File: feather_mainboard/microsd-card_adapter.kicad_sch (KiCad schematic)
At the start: 10 parts, among them J2 MEM2090-00-145-00-A

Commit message: schematic is almost done (check TODOs in schematic file)
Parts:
- removed J2: MEM2090-00-145-00-A, Custom footprints:MEM20900014500A, symbol MEM2090-00-145-00-A:MEM2090-00-145-00-A
- removed R19, R20, R21: 10kΩ, Resistor_SMD:R_0805_2012Metric_Pad1.20x1.40mm_HandSolder, symbol Device:R
- added J3: 693071020811, Custom footprints:693071020811, symbol 693071020811:693071020811
- added R15, R16, R17: 10kΩ, Resistor_SMD:R_0805_2012Metric_Pad1.20x1.40mm_HandSolder, symbol Device:R
- renumbered C8 to C11, C9 to C12, R16 to R12, R17 to R13, R18 to R14
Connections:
- net GND: now also J3.10 (GND), J3.11 (GND__1), J3.12 (GND__2), J3.13 (GND__3)
- net SD_CD: now also J3.9 (CDSW1), R17.1
- net SD_CLK: now also J3.5 (CLK)
- net SD_CS/DAT3: now also J3.2 (CD/DAT3)
- net SD_DAT1: now also J3.8 (DAT1), R15.2
- net SD_DAT2: now also J3.1 (DAT2)
- net SD_GND: now also J3.6 (VSS)
- net SD_MISO/CMD: now also J3.3 (CMD)
- net SD_MOSI/DAT0: now also J3.7 (DAT0), R16.2
- net SD_VCC: now also J3.4 (VDD)
- net VCC: now also R15.1, R16.1, R17.2
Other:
- moved on the sheet: C11, C12

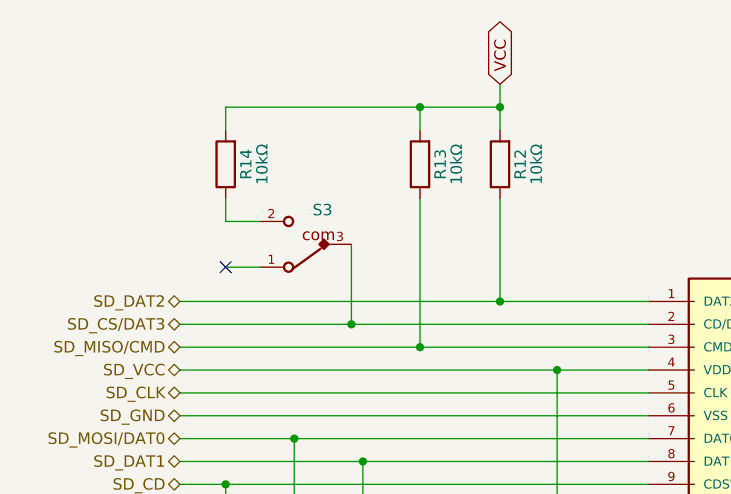
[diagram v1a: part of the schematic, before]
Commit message: changed footprints location to match the new folder. TODO: check if the path is working on another computer
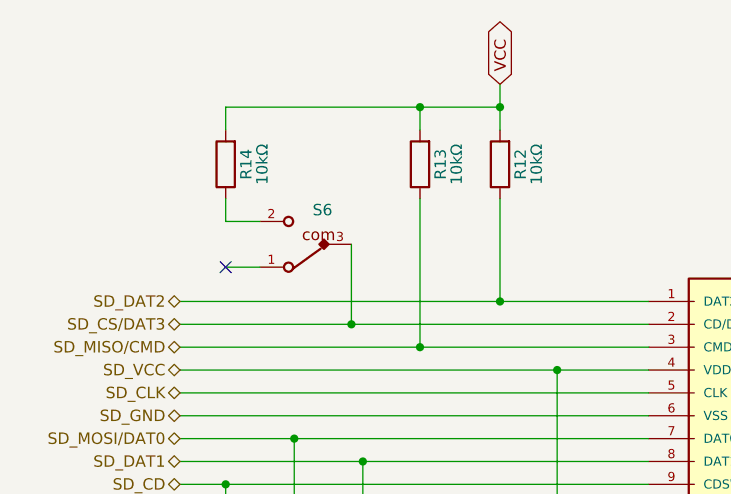
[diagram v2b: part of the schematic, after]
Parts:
- C11, C12: footprint footprints:WCAP-CSGP_1210_H2.0 -> Custom footprints:WCAP-CSGP_1210_H2.0
- renumbered S3 to S6
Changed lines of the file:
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@@
 			)
 		)
-		(property "Footprint" "footprints:WCAP-CSGP_1210_H2.0"
+		(property "Footprint" "Custom footprints:WCAP-CSGP_1210_H2.0"
 			(at 121.92 123.19 0)
 			(effects
@@
 	)
 	(symbol
+		(lib_name "WCAP-CSGP_1210_H2.0_1")
 		(lib_id "WCAP-CSGP_1210_H2.0:WCAP-CSGP_1210_H2.0")
 		(at 130.81 123.19 270)
@@
 			)
 		)
-		(property "Footprint" "footprints:WCAP-CSGP_1210_H2.0"
+		(property "Footprint" "Custom footprints:WCAP-CSGP_1210_H2.0"
 			(at 130.81 123.19 0)
 			(effects
@@
 		(on_board yes)
 		(dnp no)
-		(property "Reference" "S3"
+		(property "Reference" "S6"
 			(at 103.632 81.28 0)
 			(effects
@@
 			(project "feather_mainboard"
 				(path "/e1e12730-ab4f-45db-8b66-c1e0f78e2f00/6bb461df-e058-49ab-990d-543fb2df67dd"
-					(reference "S3")
+					(reference "S6")
 					(unit 1)
 				)

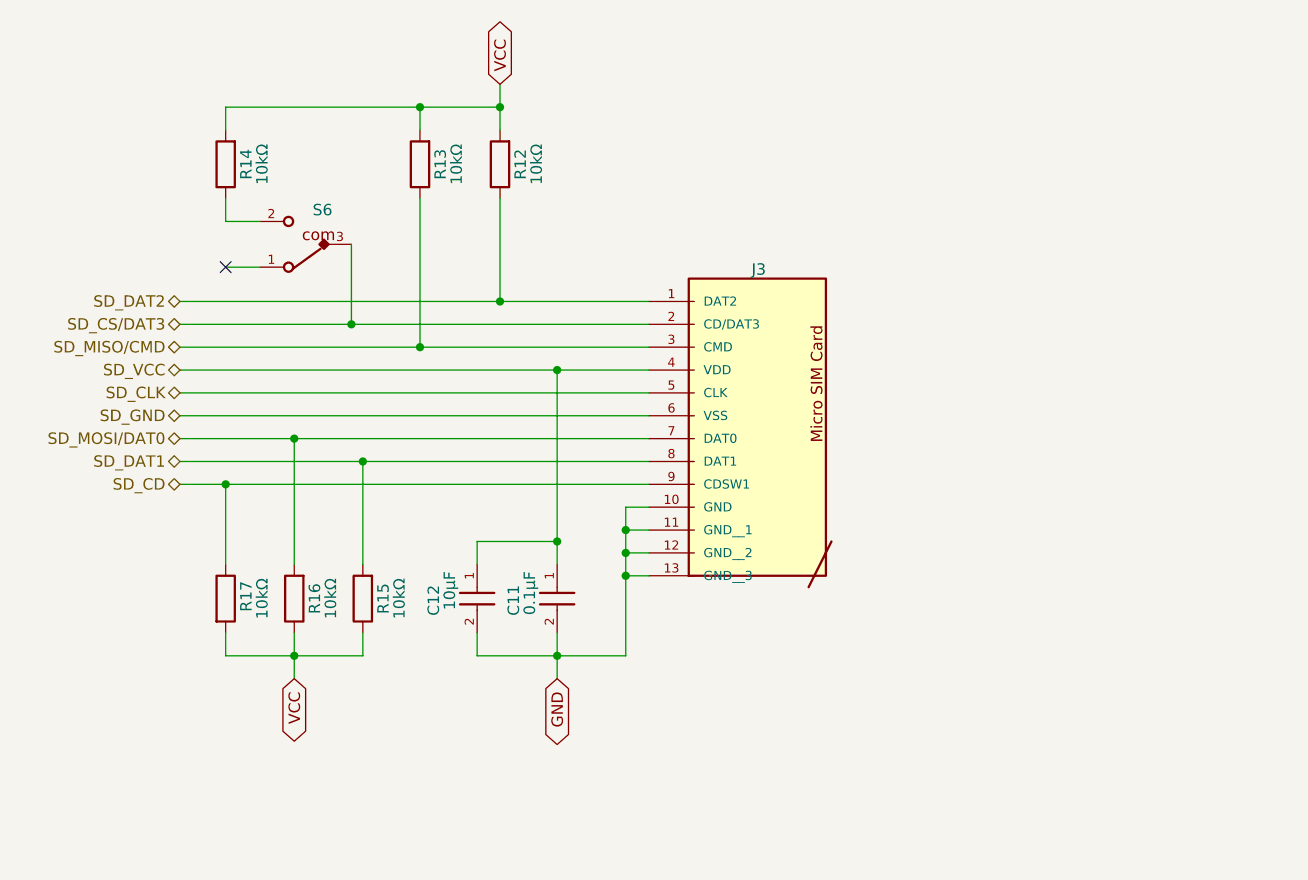
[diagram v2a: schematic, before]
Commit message: added daughter board
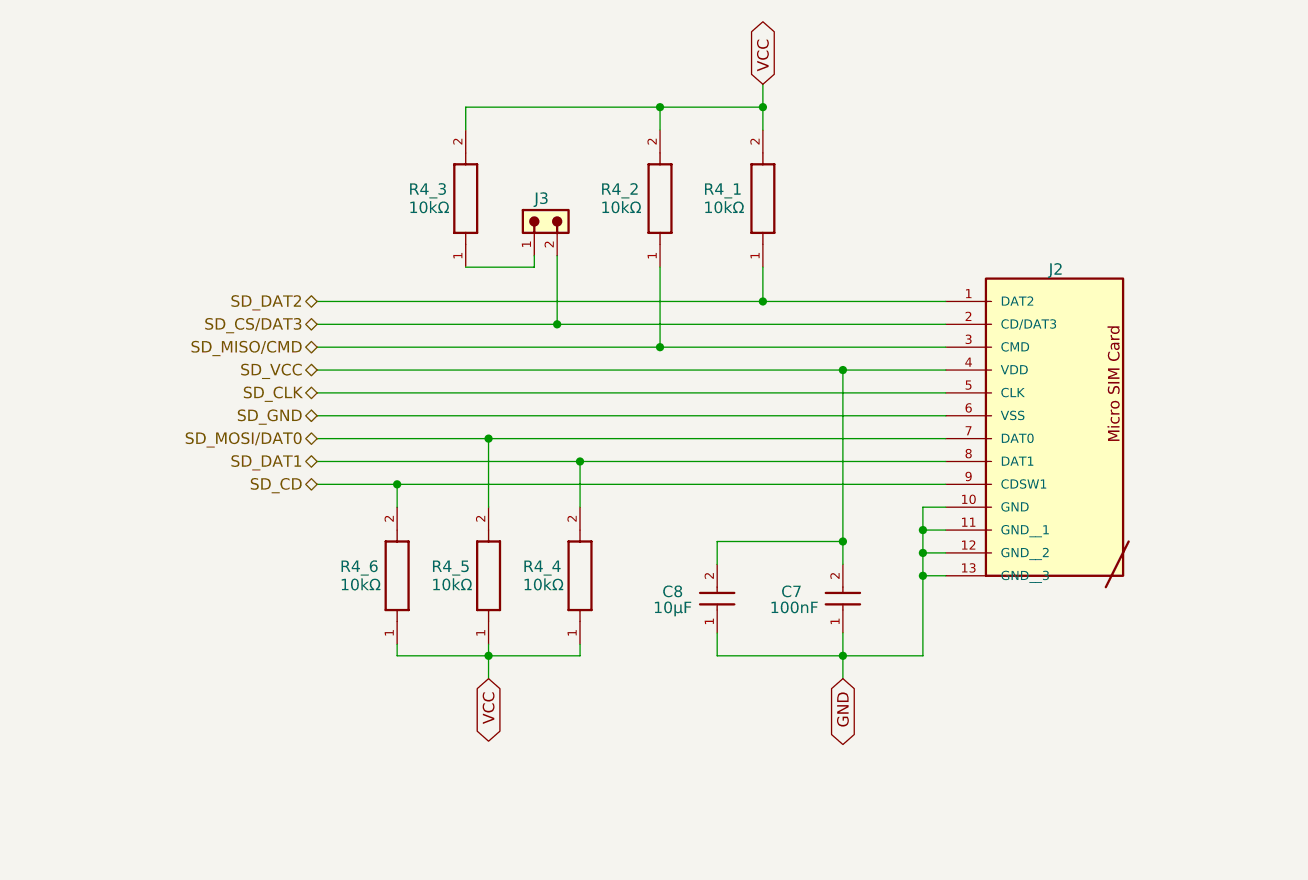
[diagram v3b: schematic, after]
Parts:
- removed C11: 0.1µF, Custom footprints:WCAP-CSGP_1210_H2.0, symbol WCAP-CSGP_1210_H2.0:WCAP-CSGP_1210_H2.0
- removed C12: 10µF, Custom footprints:WCAP-CSGP_1210_H2.0, symbol WCAP-CSGP_1210_H2.0:WCAP-CSGP_1210_H2.0
- removed R12, R13, R14, R15, R16, R17: 10kΩ, Resistor_SMD:R_0805_2012Metric_Pad1.20x1.40mm_HandSolder, symbol Device:R
- removed S6: 450405020524, Custom footprints:450405020524, symbol 450405020524:450405020524
- added C7: 100nF, Custom footprints:WCAP-CSGP_0603_R, symbol WCAP-CSGP_0603:WCAP-CSGP_0603
- added C8: 10µF, Custom footprints:WCAP-CSGP_0603_R, symbol WCAP-CSGP_0603:WCAP-CSGP_0603
- added J3: 61300211121, Custom footprints:61300211121, symbol 6130XX11121_61300211121:6130XX11121_61300211121
- added R4_1, R4_2, R4_3, R4_4, R4_5, R4_6: 10kΩ, Custom footprints:WRIS-RSKS_0603_REFLOW, symbol WRIS-RSKS_0603:WRIS-RSKS_0603
- renumbered J3 to J2
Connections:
- net GND: now also C7.1, C8.1
- net SD_CD: now also R4_6.2
- net SD_CS/DAT3: now also J3.2
- net SD_DAT1: now also R4_4.2
- net SD_DAT2: now also R4_1.1
- net SD_MISO/CMD: now also R4_2.1
- net SD_MOSI/DAT0: now also R4_5.2
- net SD_VCC: now also C7.2, C8.2
- net VCC: now also R4_1.2, R4_2.2, R4_3.2, R4_4.1, R4_5.1, R4_6.1
- new net: J3.1, R4_3.1
- no-connect marks 1 -> 0
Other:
- moved on the sheet: J2

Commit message: finished mainboard design, need to do the routing
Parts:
- renumbered C7 to C1_4, C8 to C2_2, J2 to J4, J3 to J5, R4_5 to R1_10, R4_6 to R1_11, R4_1 to R1_6, R4_2 to R1_7, R4_3 to R1_8, R4_4 to R1_9
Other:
- moved on the sheet: C1_4, C2_2, J4, R1_10, R1_11, R1_6, R1_7, R1_8, R1_9

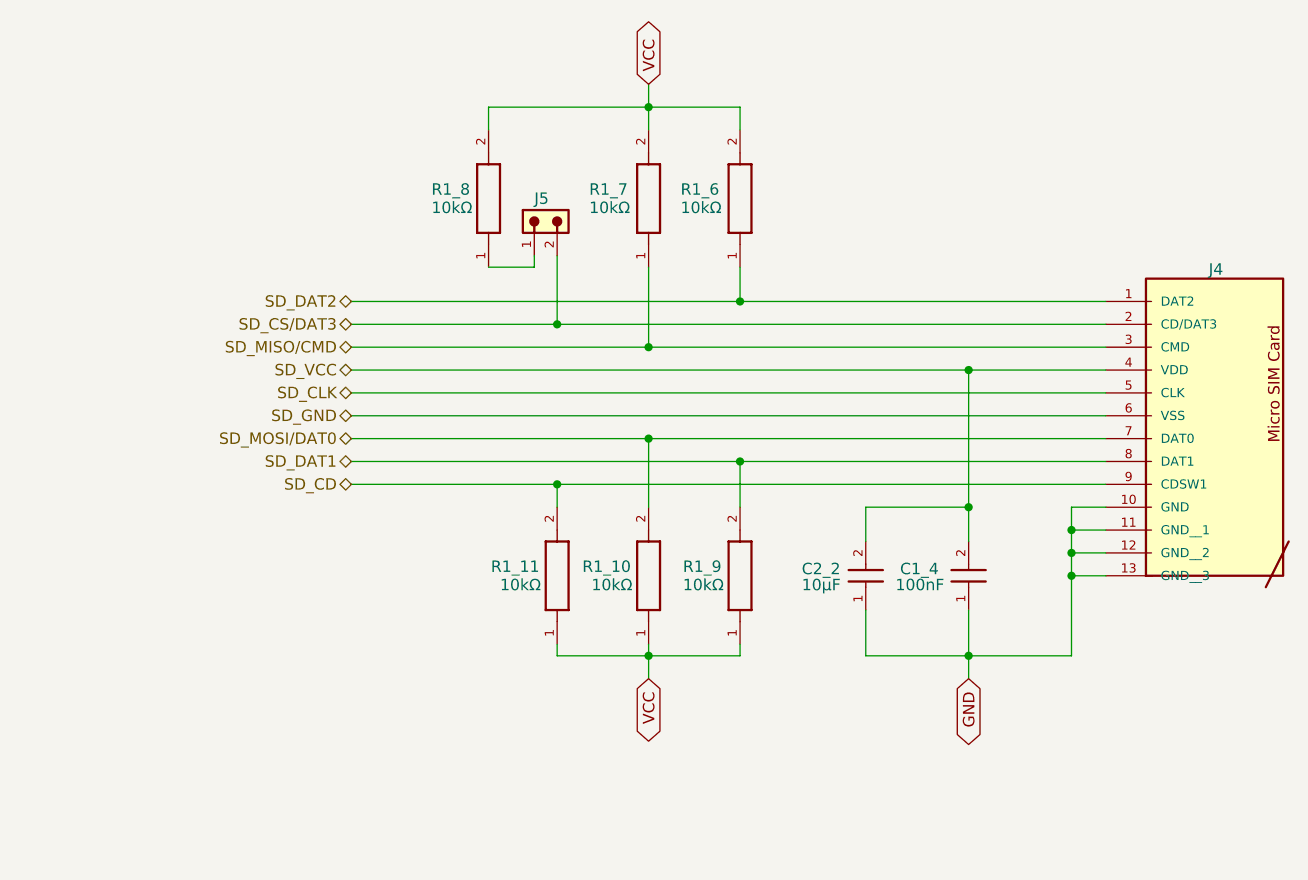
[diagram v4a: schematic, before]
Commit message: added pins for the sd connections
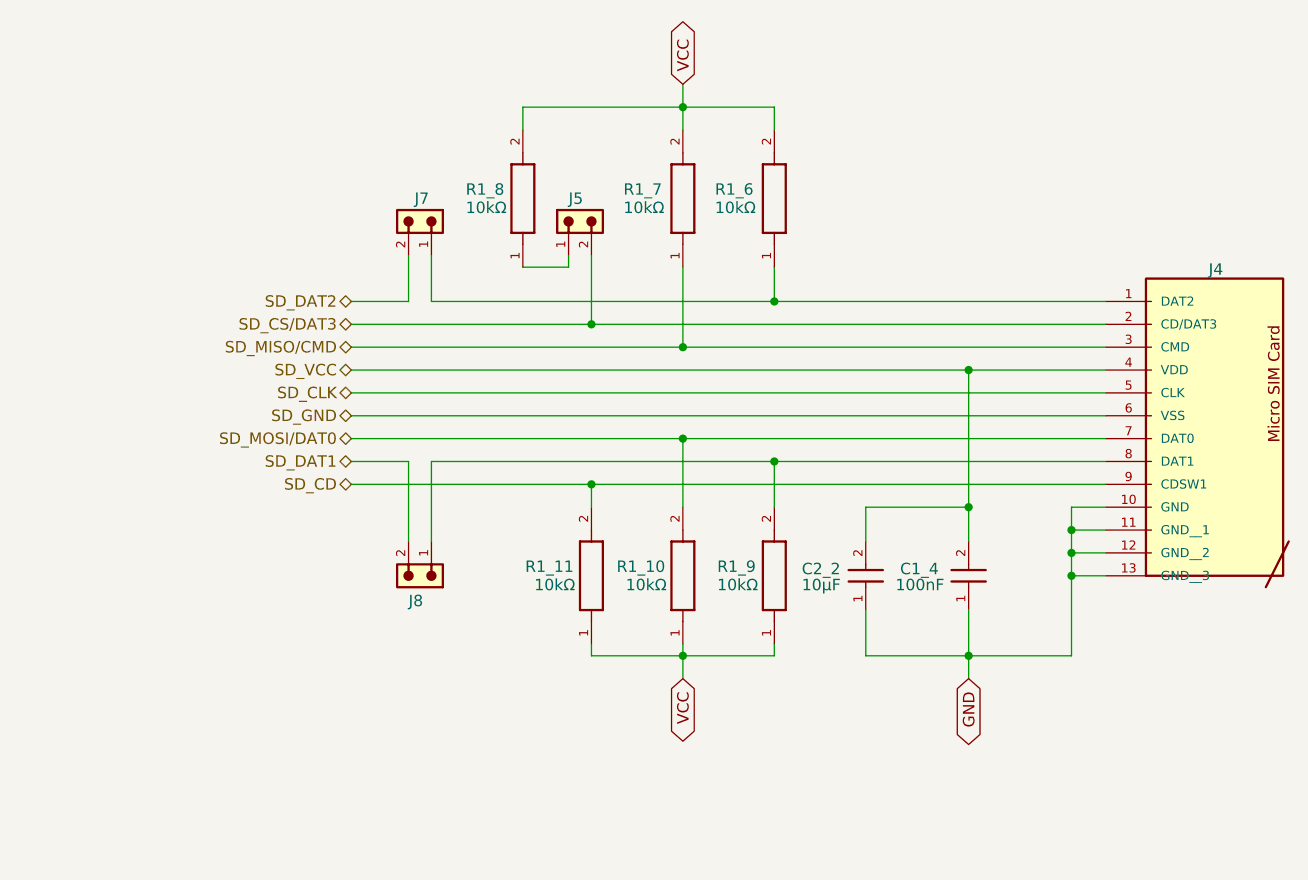
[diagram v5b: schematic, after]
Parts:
- added J7, J8: 61300211121, Custom footprints:61300211121, symbol 6130XX11121_61300211121:6130XX11121_61300211121
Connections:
- net SD_DAT1: now also J8.2; no longer J4.8 (DAT1), R1_9.2
- net SD_DAT2: now also J7.2; no longer J4.1 (DAT2), R1_6.1
- new net: J4.8 (DAT1), J8.1, R1_9.2
- new net: J4.1 (DAT2), J7.1, R1_6.1
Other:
- moved on the sheet: J5, R1_10, R1_11, R1_6, R1_7, R1_8, R1_9

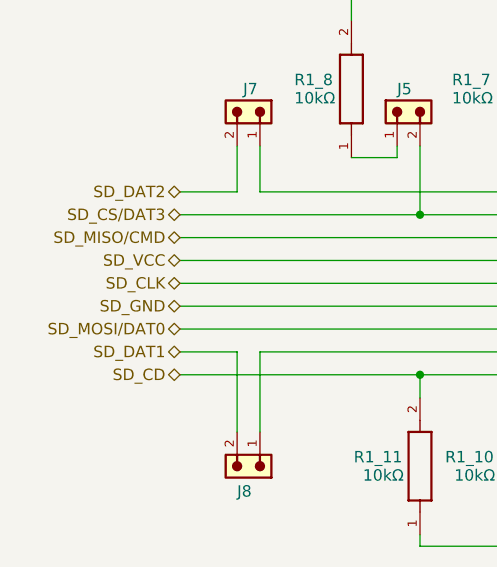
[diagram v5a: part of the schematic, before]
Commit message: Corrected/switched the names of MISO and MOSI pins
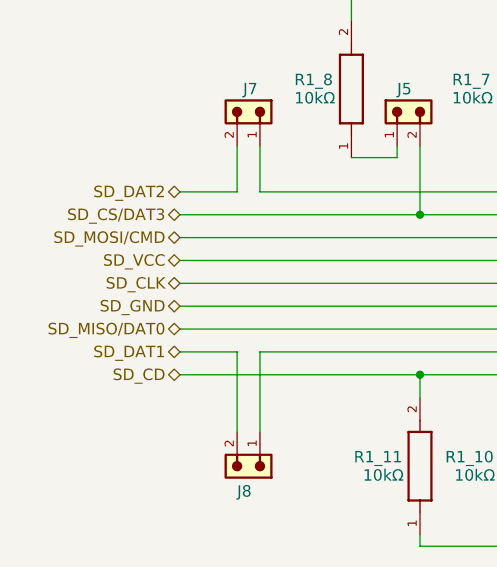
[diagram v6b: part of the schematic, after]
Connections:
- net SD_MISO/CMD renamed SD_MOSI/CMD
- net SD_MOSI/DAT0 renamed SD_MISO/DAT0
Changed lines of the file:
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@@
 		)
 	)
-	(hierarchical_label "SD_MOSI{slash}DAT0"
+	(hierarchical_label "SD_MISO{slash}DAT0"
 		(shape bidirectional)
 		(at 107.95 106.68 180)
@@
 		)
 	)
-	(hierarchical_label "SD_MISO{slash}CMD"
+	(hierarchical_label "SD_MOSI{slash}CMD"
 		(shape bidirectional)
 		(at 107.95 96.52 180)

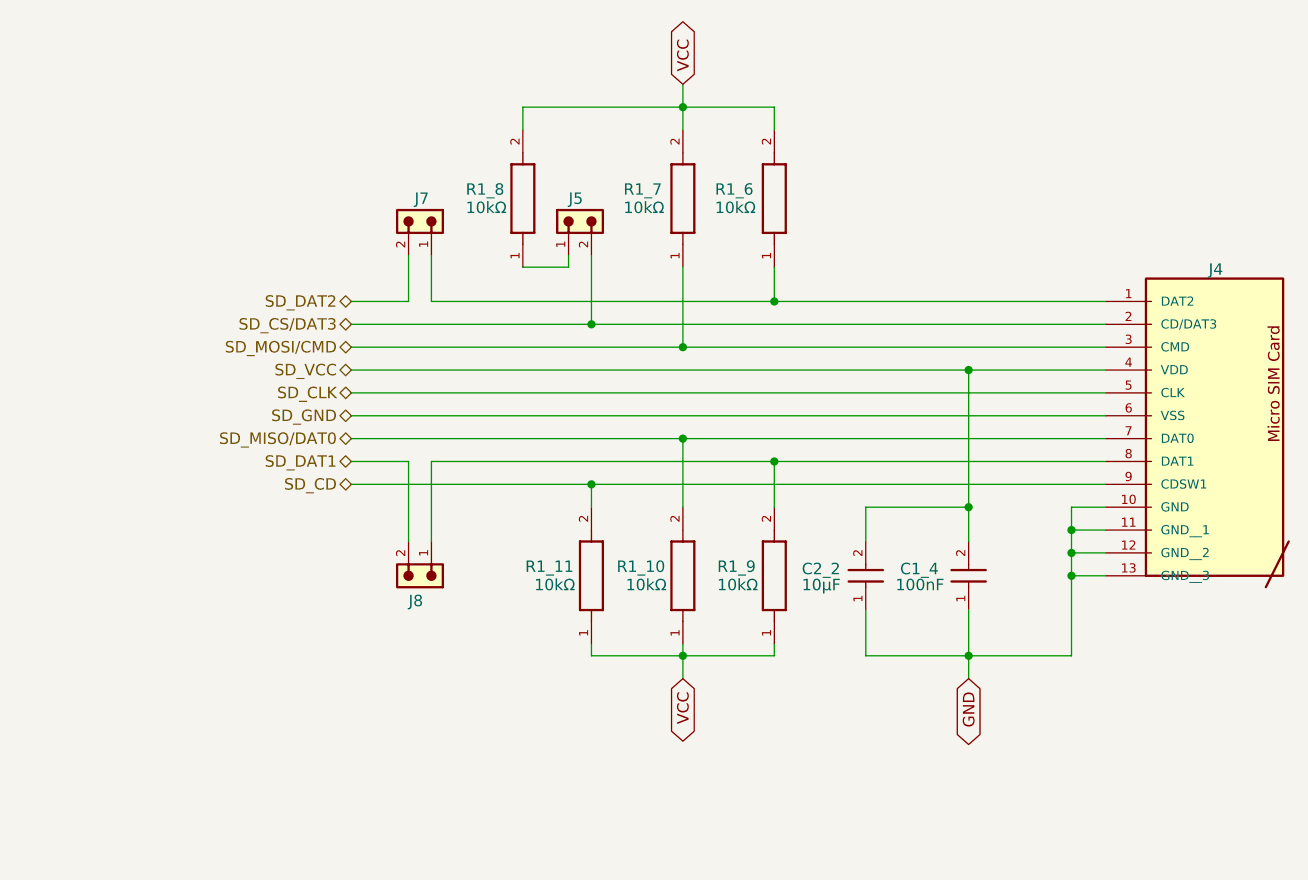
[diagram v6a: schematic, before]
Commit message: Added V1.1: added a Shottky diode to block the parasitic feedback into the system from the SD adapter; routed the SD adapter pull-ups to the SD Vcc and not the uC Vcc; updated silkscreen text; cleaned routing overall; more vias and more ground plane coverage
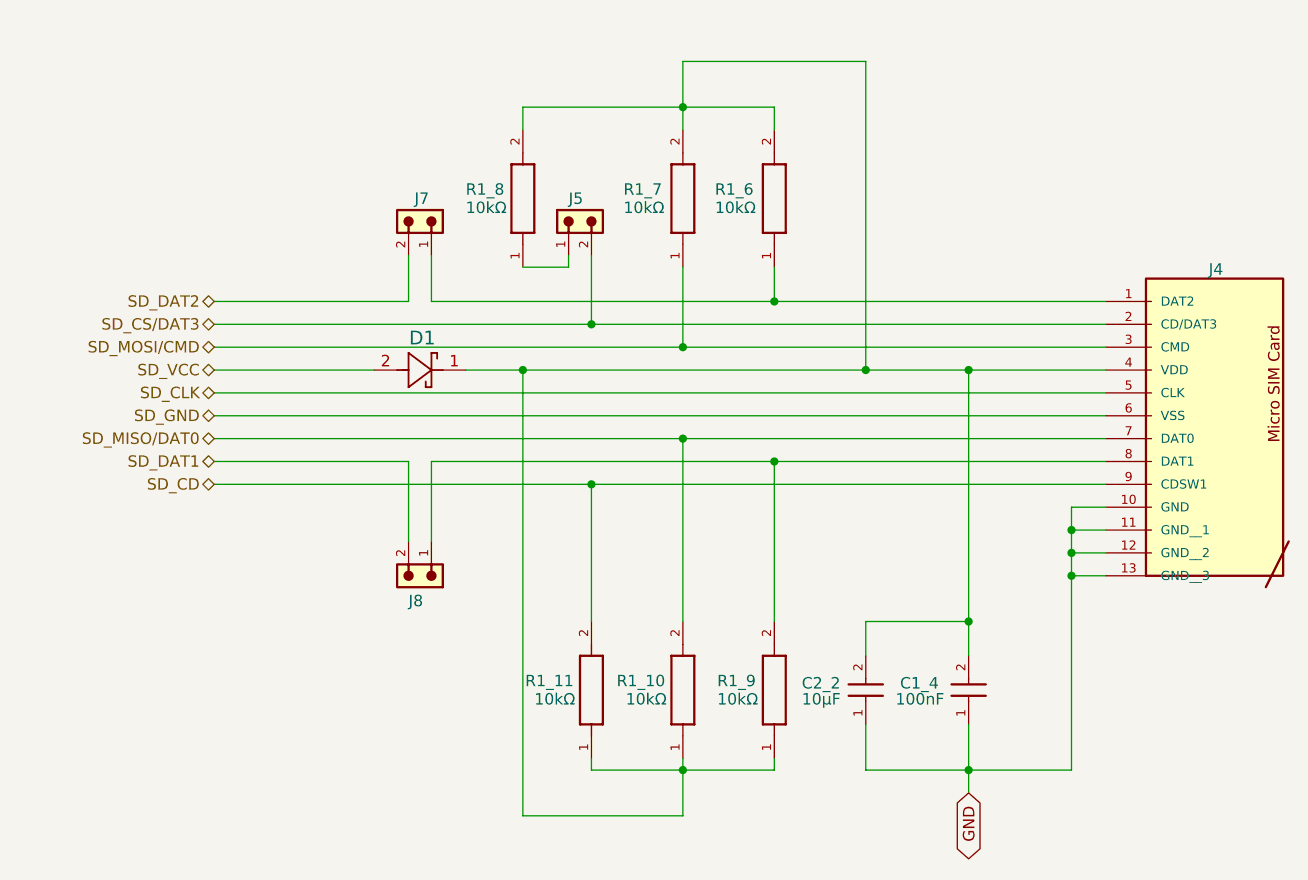
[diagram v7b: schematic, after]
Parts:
- added D1: PMEG6010CEH_115, Custom footprints:SDO_SOD123F_NEX, symbol SDO_SOD123F_NEX:PMEG6010CEH_115
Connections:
- net SD_VCC: now also D1.2; no longer C1_4.2, C2_2.2, J4.4 (VDD)
- net VCC: no longer names the net of R1_10.1, R1_11.1, R1_6.2, R1_7.2, R1_8.2, R1_9.1
- net VCC: now also C1_4.2, C2_2.2, J4.4 (VDD), D1.1
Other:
- moved on the sheet: C1_4, C2_2, R1_10, R1_11, R1_9
